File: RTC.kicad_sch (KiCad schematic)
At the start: 12 parts, among them IC7 74LVC1G07QSE-7, J7 Molex 470531000, U1 PCF8563T, U10 EMC2301-1-ACZL-TR, Y2 X32K768S301

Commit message: small changes for ravi
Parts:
- removed Y2: X32K768S301, Crystal:Crystal_SMD_3215-2Pin_3.2x1.5mm, symbol Device:Crystal_Small
- added BT1: Battery_Cell, symbol Device:Battery_Cell
- added D6: BAT54C-7-F, Package_TO_SOT_SMD:SOT-23, symbol Diode:BAT54C
- added Y6: ECS-.327-6, ECS327616RTR, symbol ECS-.327-6-16R-TR:ECS-.327-6-16R-TR
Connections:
- net +3.3V_PWR: now also D6.2; no longer C20.1, U1.8 (VDD)
- net GND: now also BT1.2 (-)
- net at U1.2 (OSCO): now also Y6.2
- net at U1.1 (OSCI): now also Y6.1
- new net: BT1.1 (+), D6.1
- new net: C20.1, D6.3, U1.8 (VDD)
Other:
- note added: "RTC alarms can wake up the CM4 when off or shutdown. If CM4 is already awake when alarm triggers, CM4 is reset. This can be used as watchdog reset."
- note removed: "RTC alarms can be used to wake up the CM4 when off or shutdown. If CM4 is already awake when alarm triggers, CM4 is reset. This can be used as watchdog reset"

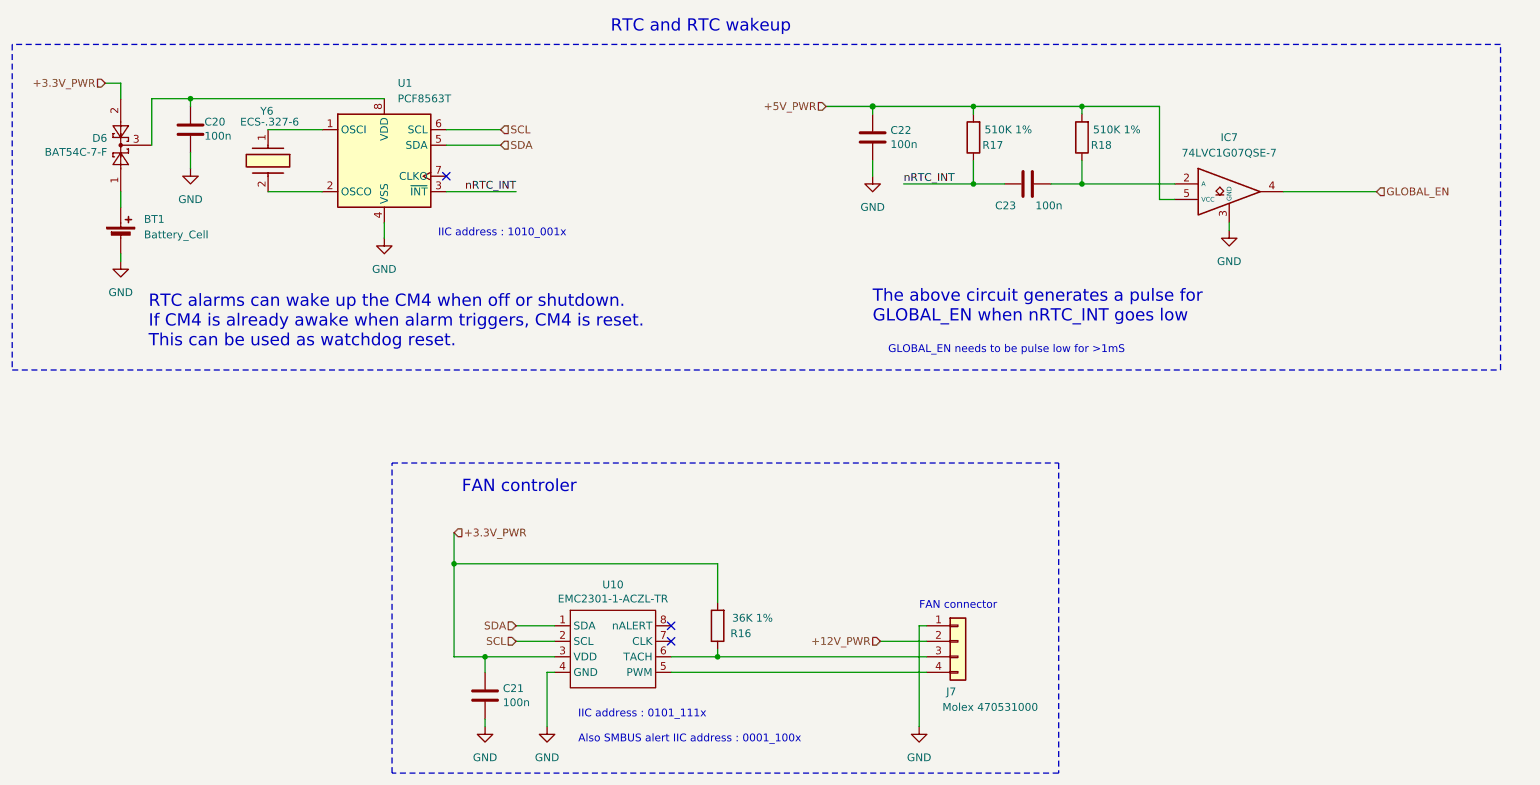
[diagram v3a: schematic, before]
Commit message: added parts to almost everything (except can xtal and fuses)
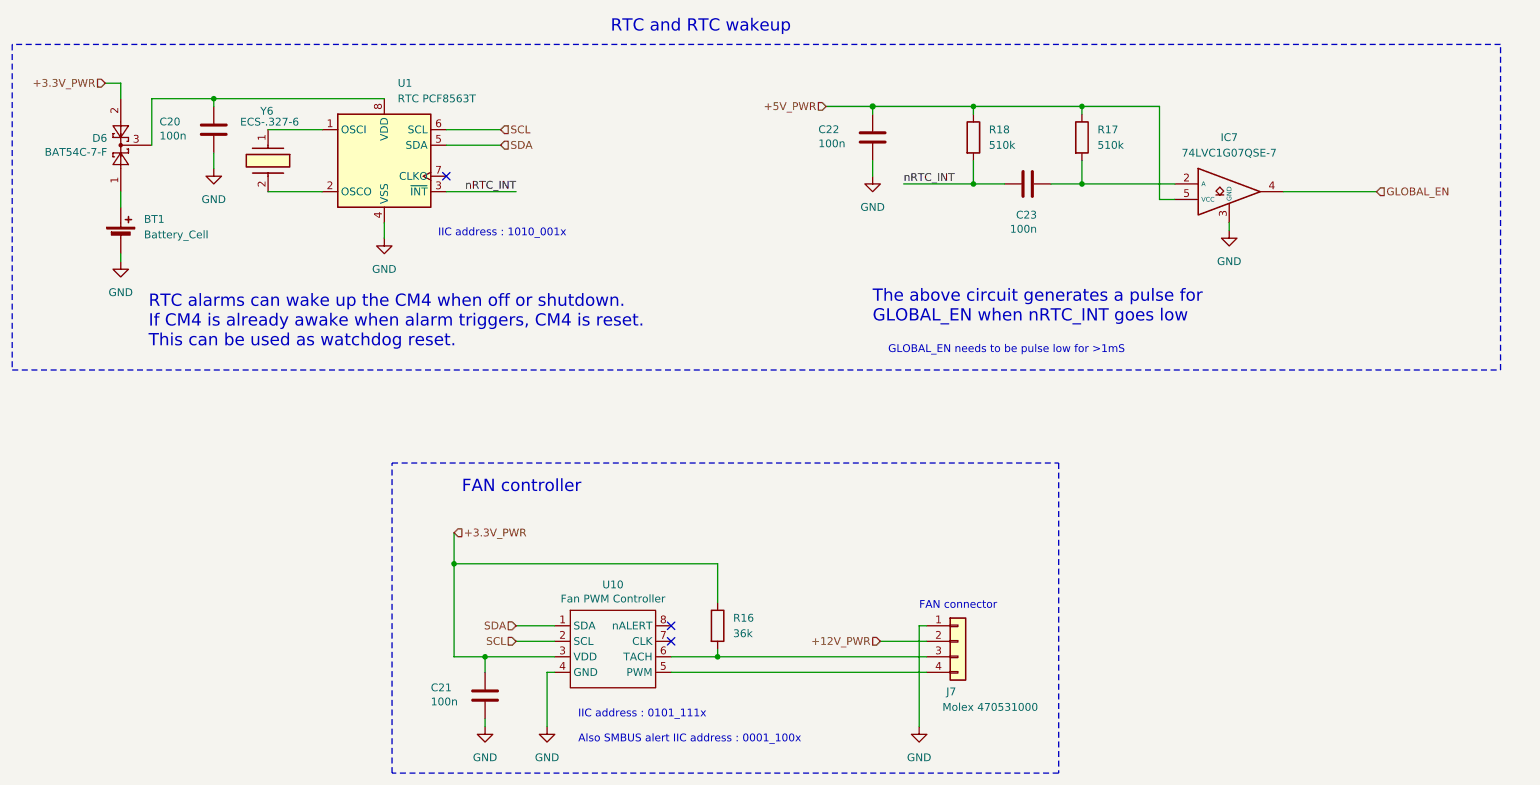
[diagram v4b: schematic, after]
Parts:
- BT1: Field5 CR2032 20mm cell -> (none); P/N (none) -> 1086
- C20, C21, C22, C23: footprint Capacitor_SMD:C_0402_1005Metric -> Capacitor_SMD:C_0805_2012Metric; Field4 Farnell -> (none); Field5 2611911 -> (none); Field6 RM EMK105 B7104KV-F -> (none); Field7 TAIYO YUDEN EUROPE GMBH -> (none); Field8 110091611 -> (none); P/N (none) -> C0805C104M5RACTU; Part Description 0.1uF 10% 16V Ceramic Capacitor X7R 0402 (1005 Metric) -> (none)
- D6: Field4 Farnell -> (none); Field5 2306010 -> (none); Field6 BAT54C-7-F -> (none); Field7 Rohm -> (none); P/N (none) -> BAT54C-7-F; Part Description Diode Array 1 Pair Common Cathode Schottky 30V 200mA (DC) S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 -> (none)
- IC7: Arrow Part Number 74LVC1G07QSE-7 -> (none); Arrow Price/Stock https://www.arrow.com/en/products/74lvc1g07qse-7/diodes-inc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 -> (none); Height 1.1 -> (none); Manufacturer_Name Diodes Incorporated -> (none); Manufacturer_Part_Number 74LVC1G07QSE-7 -> (none); Mouser Part Number 621-74LVC1G07QSE-7 -> (none); Mouser Price/Stock https://www.mouser.co.uk/ProductDetail/Diodes-Incorporated/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 -> (none)
- J7: Field4 Farnell -> (none); Field5 2313705 -> (none); Field6 470531000 -> (none); Field7 Molex -> (none); P/N (none) -> 470531000; Part Description Connector Header Through Hole 4 position 0.100" (2.54mm) -> (none)
- R16: value 36K 1% -> 36k; Field4 Farnell -> (none); Field5 1458788 -> (none); Field6 MCR01MZPF3602 -> (none); Field7 Rohm -> (none); P/N (none) -> MCR01MZPF3602; Part Description Resistor 36K M1005 1% 63mW -> (none)
- R17, R18: value 510K 1% -> 510k; Field4 Farnell -> (none); Field5 1458807 -> (none); Field6 MCR01MZPF5103 -> (none); Field7 Rohm -> (none); P/N (none) -> MCR01MZPF5103; Part Description Resistor 510K M1005 1% 63mW -> (none)
- U1: value PCF8563T -> RTC PCF8563T; P/N (none) -> PCF8563T
- U10: value EMC2301-1-ACZL-TR -> Fan PWM Controller; Field4 Digikey -> (none); Field5 EMC2301-1-ACZL-CT-ND -> (none); Field6 EMC2301-1-ACZL-TR -> (none); Field7 Microchip -> (none); P/N (none) -> EMC2301-1-ACZL-TR; Part Description Motor Driver PWM 8-MSOP -> (none)
- Y6: footprint ECS327616RTR -> Controls_Pi:ECS327616RTR; Arrow Part Number ECS-.327-6-16R-TR -> (none); Arrow Price/Stock https://www.arrow.com/en/products/ecs-.327-6-16r-tr/ecs-int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 -> (none); Height 0.5 -> (none); Manufacturer_Name ECS -> (none); Manufacturer_Part_Number ECS-.327-6-16R-TR -> (none); Mouser Part Number 520-ECS-.327-6-16RTR -> (none); Mouser Price/Stock https://www.mouser.co.uk/ProductDetail/ECS/ECS-.327-6-16R-T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 -> (none); P/N (none) -> ECS-.327-6-16R-TR
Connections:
- net +3.3V_PWR: now also R16.1; no longer R16.2
- net +5V_PWR: now also R17.1, R18.1; no longer R17.2, R18.2
- net nRTC_INT: now also C23.1, R18.2; no longer C23.2, R17.1
- net at J7.3 (Pin_3), U10.6 (TACH): now also R16.2; no longer R16.1
- new net: C23.2, IC7.2 (A), R17.2
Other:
- note added: "FAN controller"
- note removed: "FAN controler"

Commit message: fixed cap sizes, added remaining parts, fixed rtc battery
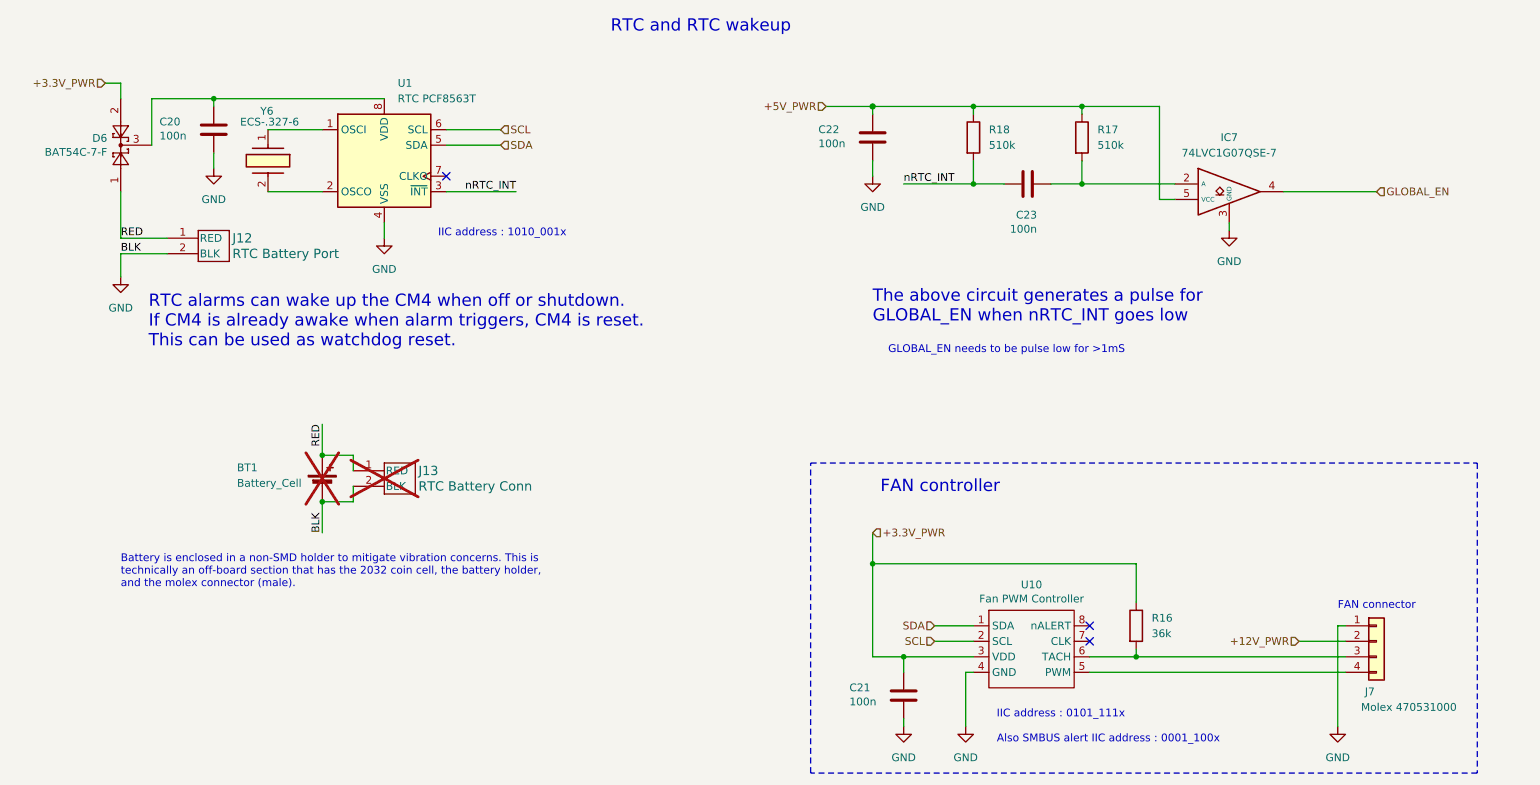
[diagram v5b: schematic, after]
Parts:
- added J12: RTC Battery Port, Controls_Pi:CONN02_530470210_MOL, symbol 530470210:530470210
- added J13: RTC Battery Conn, symbol 530470210:530470210
- BT1: now not fitted
- IC7: footprint SOT65P210X110-5N -> Controls_Pi:SOT65P210X110-5N; P/N (none) -> 74LVC1G07QSE-7
- R16: footprint Resistor_SMD:R_0402_1005Metric -> Resistor_SMD:R_0805_2012Metric; P/N MCR01MZPF3602 -> AC0805FR-0736KL
- R17, R18: footprint Resistor_SMD:R_0402_1005Metric -> Resistor_SMD:R_0805_2012Metric; P/N MCR01MZPF5103 -> RC0805FR-07510KL
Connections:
- net GND: now also J12.2 (BLK), J13.2 (BLK)
- net RED: now reaches BT1.1 (+), D6.1
- net RED: now also J12.1 (RED), J13.1 (RED)
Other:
- note added: "Battery is enclosed in a non-SMD holder to mitigate vibration concerns. This is technically an off-board section that has the 2032 coin cell, the battery holder, and the molex connector (male)."
- moved on the sheet: C21, J7, R16, U10

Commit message: review committee changes implmented
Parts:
- removed C22, C23: 100n, Capacitor_SMD:C_0805_2012Metric, symbol Device:C
- removed IC7: 74LVC1G07QSE-7, Controls_Pi:SOT65P210X110-5N, symbol 74LVC1G07QSE-7:74LVC1G07QSE-7
- removed R17, R18: 510k, Resistor_SMD:R_0805_2012Metric, symbol Device:R
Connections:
- net nRTC_INT: no longer names the net of U1.3 (~{INT})
- no-connect marks 3 -> 4
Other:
- note added: "RTC alarms can wake up the CM4 when off or shutdown (using the INT pin). If CM4 is already awake when alarm triggers, CM4 is reset. This can be used as watchdog reset. We are not going to utilize this!"
- note removed: "GLOBAL_EN needs to be pulse low for >1mS"
- note removed: "RTC alarms can wake up the CM4 when off or shutdown. If CM4 is already awake when alarm triggers, CM4 is reset. This can be used as watchdog reset."
- note removed: "The above circuit generates a pulse for GLOBAL_EN when nRTC_INT goes low"

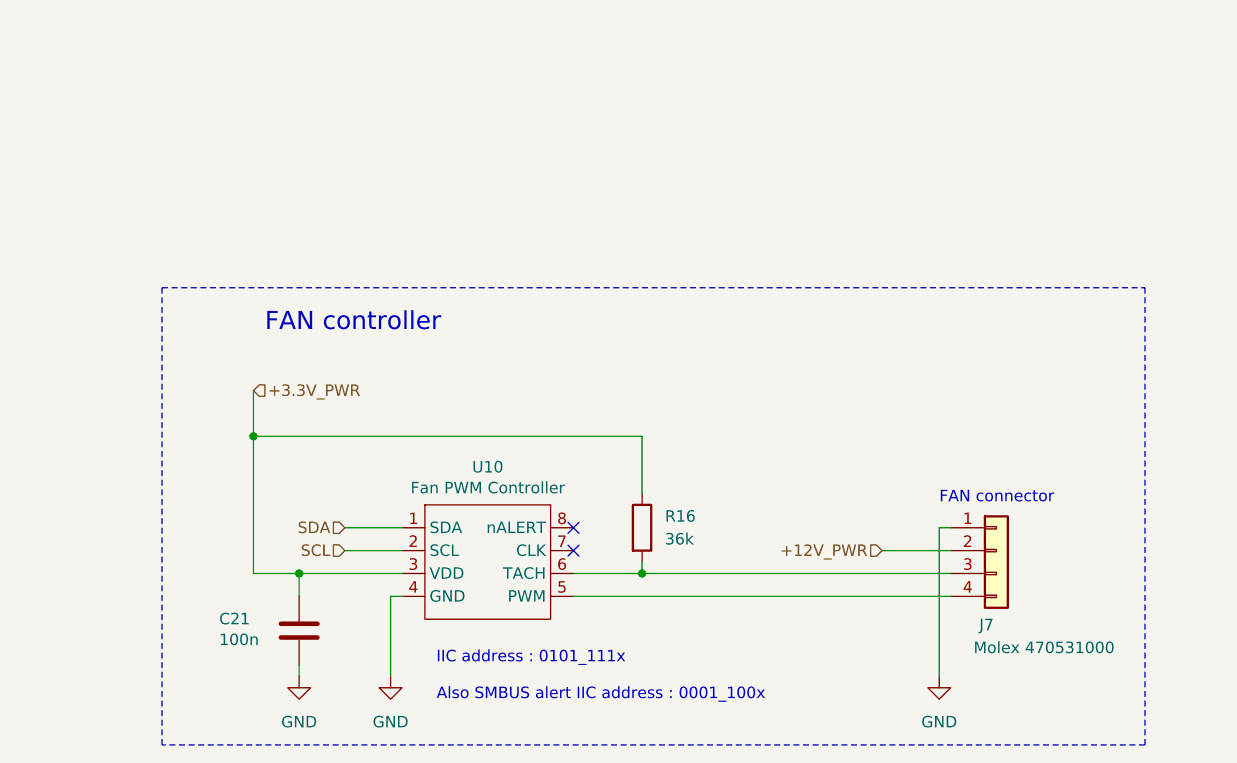
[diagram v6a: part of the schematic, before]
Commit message: fixed relevant erc errors
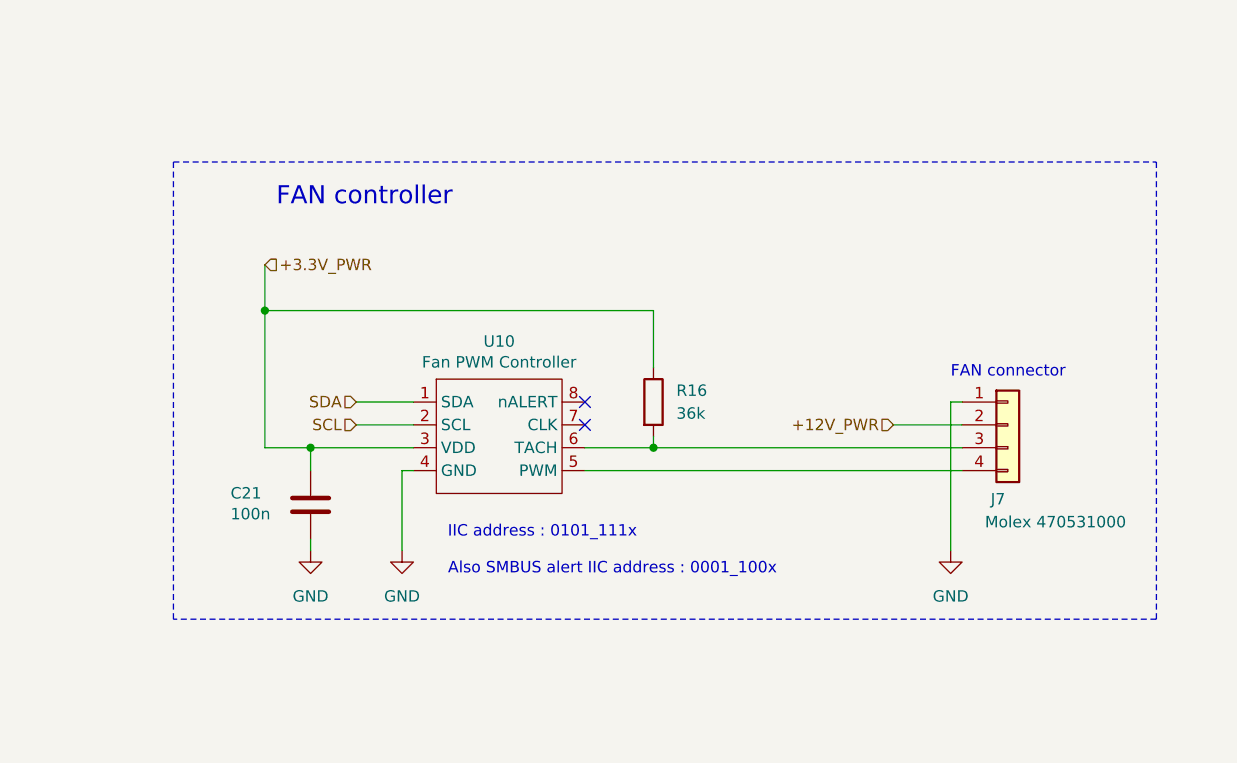
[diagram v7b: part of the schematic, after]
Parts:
- J12: footprint Controls_Pi:CONN02_530470210_MOL -> CONN02_530470210_MOL
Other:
- moved on the sheet: C21, J7, R16, U10
